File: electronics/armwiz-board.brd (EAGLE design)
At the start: 98.8 x 51 mm, 80 parts, among them J1 MICROSD, J2 CORTEX_DEBUGSMD, U1 STM32F10XRXT6, U4 MIC5219-3.3V, X2 M12_BOTTOM_CONTACTS_FPC_1MM, Y1 32.768kHz, Y3 32.768kHz

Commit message: Crazy routing work.
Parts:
- moved R8 18.2 mm to (90.0, 18.5)
- moved R11 4.92 mm to (90.0, 17.0)
- moved R19 3.91 mm to (52.0, 14.8), turned to 180 degrees
- moved C35 3.58 mm to (44.0, 14.8)
- moved R12 2.69 mm to (90.0, 15.5)
- moved SJ2 2.30 mm to (18.2, 23.5)
- moved R25 2.25 mm to (82.5, 9.75), turned to 0 degrees
- moved C36 1.90 mm to (41.2, 14.8)
- moved C19 1.50 mm to (31.5, 6.25)
- moved C20 1.50 mm to (36.5, 6.00)
- moved Y1 1.50 mm to (34.0, 6.25)
- moved C8 1.03 mm to (32.0, 9.25)
- moved C6 1.00 mm to (37.0, 3.50)
- moved C9 1.00 mm to (32.0, 3.25)
- moved R13 1.00 mm to (58.5, 3.00)
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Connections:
- removed net PA1: U1.15
- removed net PC2: U1.10
- removed net PC3: U1.11
- net SW_A: now also U1.15
- net SW_B: now also U1.11
- net SW_C: now also U1.10
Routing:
- net GND: track 338.1 -> 34.9 mm, vias 19 -> 27
- net SW_A: track 0.00 -> 101.9 mm
- net SW_B: track 0.00 -> 87.7 mm
- net SW_C: track 0.00 -> 79.9 mm
- net RTC_BAT: track 24.8 -> 70.1 mm
- net 3.3V: track 25.0 -> 58.0 mm, vias 8 -> 18
- net LCD_A0_(GPIO): track 0.00 -> 29.2 mm, vias 0 -> 2
- net NRST: track 0.00 -> 18.4 mm, vias 0 -> 1
- net BOOT0: track 0.00 -> 14.2 mm, vias 0 -> 1
- net USART2_TX: track 88.0 -> 74.5 mm
- net LCD_BL_(GPIO): track 32.5 -> 44.7 mm, vias 1 -> 4
- net SW_PWR_(SYS_WKUP): track 8.20 -> 18.4 mm, vias 0 -> 1
- net SPI1_MISO: track 59.5 -> 67.3 mm
- net CAN_RX: track 104.2 -> 98.4 mm
- net LCD_RST_(GPIO): track 33.9 -> 30.3 mm
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- added copper zone on layer 1, net GND
- removed copper zone on layer 1, net VBUS_IN

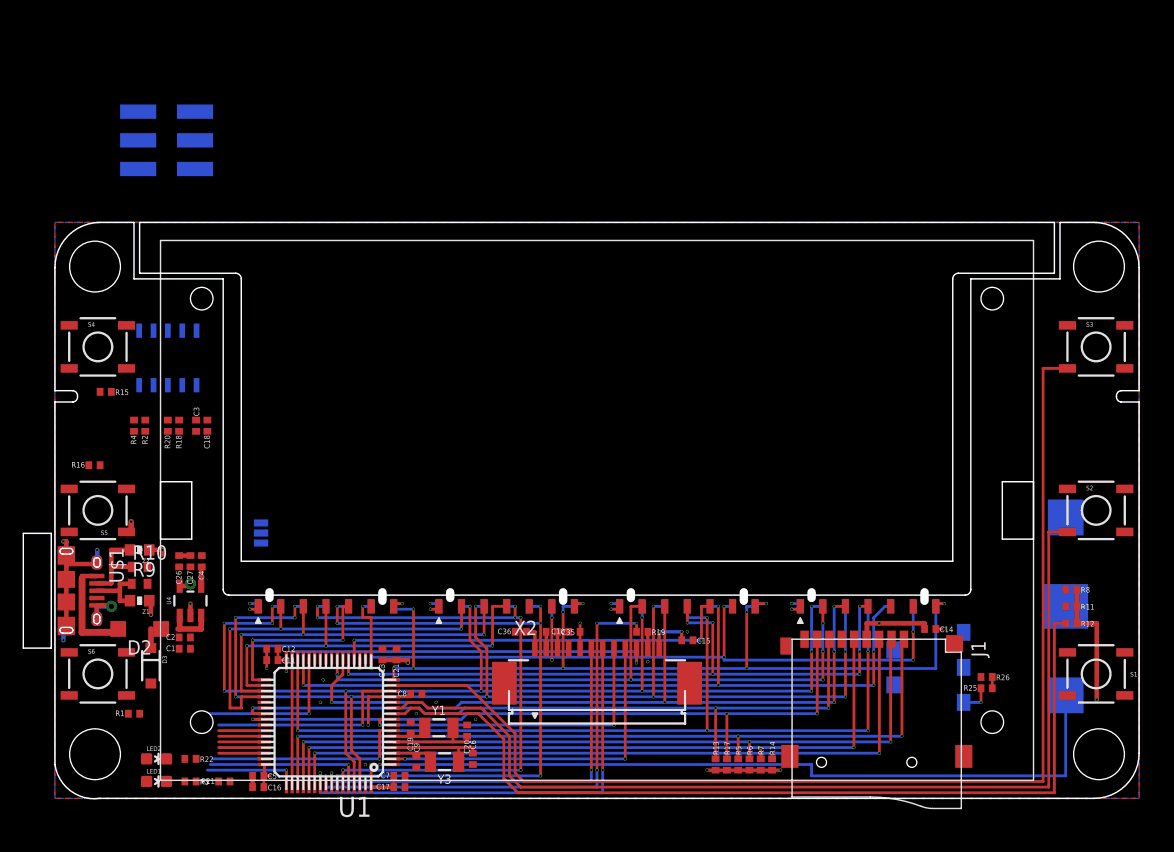
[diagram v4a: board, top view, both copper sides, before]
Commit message: Routed. Passes DRC. Added a thermocouple module.
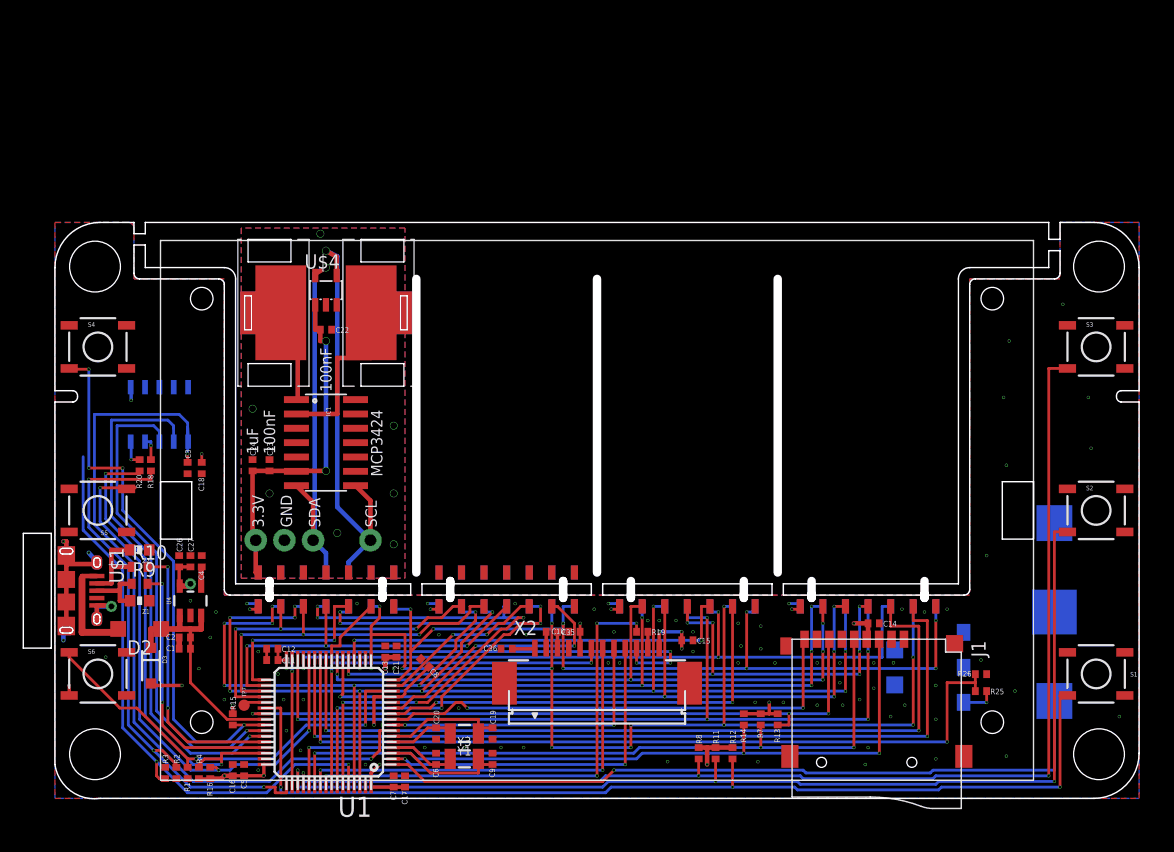
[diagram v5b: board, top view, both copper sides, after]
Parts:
- removed J25: (no value), PaxInstruments-Connectors:CONNECTORS_2X3_SMT_POSTS_T400
- removed LED1, LED2: GREEN, SparkFun-LED:LED-0603
- removed R17, R21, R5, R6: 10K, PaxInstruments-RCL:0402
- removed R22: 360R, PaxInstruments-RCL:0402
- removed SJ2: (no value), SparkFun-Retired:SJ_3
- added C22, C23: 100nF, PaxInstruments-RCL:0402
- added C24: 1uF, PaxInstruments-RCL:0402
- added IC1: MCP3424, PaxInstruments-DigitalIC:SO14
- added MODULE5, MODULE6: PI-module-male, PaxInstruments-Connectors:M07X2_2MM_EDGE
- added TP1, TP2, TP3, TP4: (no value), PaxInstruments-Connectors:M01_TH
- added TP7: (no value), PaxInstruments-Connectors:PAD_1MM
- added U$4: MCP9800A0, PaxInstruments-DigitalIC:SOT23-5L
- added U$7: THERMOCOUPLE_MINI_INSIDE, PaxInstruments-Connectors:THERMOCOUPLE_CLIP_INSIDE
- added U$8: 0.25 in, PaxInstruments-Aesthetics:PAX-LOGO-0.25IN
- J1: value MICROSD -> SD_MICRO_SDIO_1BIT; device PaxInstruments-Connectors:MICROSD_1 -> PaxInstruments-Connectors:SD_MICRO_1
- R3: value 360R -> 10K
- moved U$6 60.7 mm to (67.0, 2.00)
- moved R8 36.0 mm to (57.0, 4.00), turned to 270 degrees
- moved R11 34.1 mm to (58.5, 4.00), turned to 270 degrees
- moved R12 32.1 mm to (60.0, 4.00), turned to 270 degrees
- moved R4 31.3 mm to (12.8, 2.25), turned to 270 degrees
- moved R15 31.1 mm to (15.8, 7.00), turned to 270 degrees
- moved R2 30.9 mm to (10.8, 2.25), turned to 270 degrees
- moved R16 29.1 mm to (13.8, 2.25), turned to 90 degrees
- moved C19 7.27 mm to (38.8, 5.75), turned to 270 degrees
- moved R1 7.08 mm to (11.8, 2.25), turned to 90 degrees
- moved R13 6.80 mm to (64.0, 7.00), turned to 90 degrees
- moved C9 6.75 mm to (38.8, 3.50), turned to 90 degrees
- moved J2 5.06 mm to (9.25, 34.0)
- moved C14 5.02 mm to (72.5, 15.5)
- moved R14 4.72 mm to (61.0, 7.00), turned to 90 degrees
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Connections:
- removed net (BOOT1): SJ2.2, U1.28
- removed net LED2: LED2.A
- removed net N$11: LED2.C, R22.1
- removed net N$51: MODULE3.P$11
- removed net N$57: MODULE1.P$11
- removed net N$68: MODULE2.P$9
- removed net N$69: MODULE2.P$11
- removed net N$7: LED1.C, R3.1
- removed net N$74: MODULE4.P$9
- removed net N$75: MODULE4.P$11
- removed net PA8: U1.41
- removed net PB0: U1.26
- removed net PB1: U1.27
- removed net PC0: U1.8
- removed net PC4: U1.24
- removed net PC5: U1.25
- removed net PC7: U1.38
- removed net SDIO_D1: J1.8, R17.1, U1.40
- removed net SDIO_D2: J1.1, R5.1, U1.51
- removed net SDIO_D3: J1.2, R6.1, U1.52
- removed net SW_E: R16.2, S5.3
- new net 3.3V_1: C22.2, C23.2, C24.2, IC1.6, MODULE5.P$13, TP3.P$1, U$4.1
- new net 3.3V_2: MODULE6.P$13
- new net GND_1: C22.1, C23.1, C24.1, IC1.5, IC1.9, MODULE5.P$14, TP4.P$1, U$4.2
- new net GND_2: MODULE6.P$14
- new net MOD1_GPIO1: MODULE1.P$11, U1.24
- new net MOD2_GPIO0: MODULE2.P$9, U1.15
- new net MOD2_GPIO1: MODULE2.P$11, U1.11
- new net MOD3_GPIO1: MODULE3.P$11, U1.10
- new net MOD4_GPIO0: MODULE4.P$9, U1.25
- new net MOD4_GPIO1: MODULE4.P$11, U1.27
- new net N$25: IC1.2, U$7.P$1
- new net N$26: IC1.1, U$7.P$2
- new net SCL_1: IC1.8, MODULE5.P$6, TP2.P$1, U$4.4
- new net SDA_1: IC1.7, MODULE5.P$8, TP1.P$1, U$4.5
- new net SW_E_(BOOT1): R16.2, S5.3, U1.28
- net 3.3V: no longer J25.1, LED1.A, R17.2, R5.2, R6.2, SJ2.3
- net BOOT0: now also R3.2; no longer R21.2
- net GND: now also R3.1; no longer J25.5, MODULE1.P$13, MODULE2.P$13, MODULE3.P$13, MODULE4.P$13, R21.1, R22.2, R3.2, SJ2.1
- net LCD_A0_(GPIO): now also U1.8; no longer U1.9
- net PC6: now also TP7.P$1
- net SD_DETECT: now also U1.9
- net SW_A: now also U1.52; no longer U1.15
- net SW_B: now also U1.51; no longer U1.11
- net SW_C: now also U1.38; no longer U1.10
- net SW_D: now also U1.41
- net USART1_RX: now also J2.8; no longer J25.2
- net USART1_TX: now also J2.6; no longer J25.4
- net VBAT_1/2: now also U1.26
- net VBUS: now also U1.40
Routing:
- net MOD4_GPIO1: track 0.00 -> 74.0 mm, vias 0 -> 2
- net MOD4_GPIO0: track 0.00 -> 72.5 mm, vias 0 -> 2
- net VBAT_1/2: track 1.00 -> 72.2 mm, vias 0 -> 2
- net SDIO_D2: track 68.7 -> 0.00 mm, vias 3 -> 0
- net SDIO_D3: track 66.6 -> 0.00 mm, vias 3 -> 0
- net SDIO_D1: track 61.9 -> 0.00 mm, vias 3 -> 0
- net NRST: track 18.4 -> 71.3 mm, vias 1 -> 2
- net SW_E_(BOOT1): track 0.00 -> 51.4 mm, vias 0 -> 3
- net SW_D: track 0.00 -> 48.2 mm, vias 0 -> 4
- net SD_DETECT: track 0.00 -> 43.4 mm, vias 0 -> 2
- net USART1_RX: track 4.05 -> 46.7 mm, vias 0 -> 1
- net SWCLK: track 8.45 -> 49.7 mm, vias 1 -> 3
- net SCL_1: track 0.00 -> 39.3 mm, vias 0 -> 1
- net USART1_TX: track 4.05 -> 43.1 mm, vias 0 -> 1
- net MOD3_GPIO1: track 0.00 -> 39.0 mm, vias 0 -> 2
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- added copper zone on layer 1, net GND_1
- added copper zone on layer 16, net GND_1
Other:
- outline, holes or cut-outs redrawn
- board text added: "100nF"
- board text added: "1uF"
- board text added: "3.3V"
- board text added: "GND"
- board text added: "MCP3424"
- board text added: "MCP9800"
- board text added: "SCL"
- board text added: "SDA"
